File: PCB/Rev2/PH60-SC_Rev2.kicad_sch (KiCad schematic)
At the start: 44 parts, among them J1 USB_C_Receptacle_USB2.0_14P, J2 Conn_01x02_Pin, J3 Conn_01x02_Pin, U1 nRF52840, X1 32.768kHz, X2 Crystal_Generic

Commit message: Revert to production version and add back missing BOM
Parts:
- R1, R2: now in the parts list
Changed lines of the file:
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@@
 		(unit 1)
 		(exclude_from_sim no)
-		(in_bom no)
+		(in_bom yes)
 		(on_board yes)
 		(dnp no)
@@
 		(unit 1)
 		(exclude_from_sim no)
-		(in_bom no)
-		(on_board yes)
-		(dnp no)
+		(in_bom yes)
+		(on_board yes)
+		(dnp no)

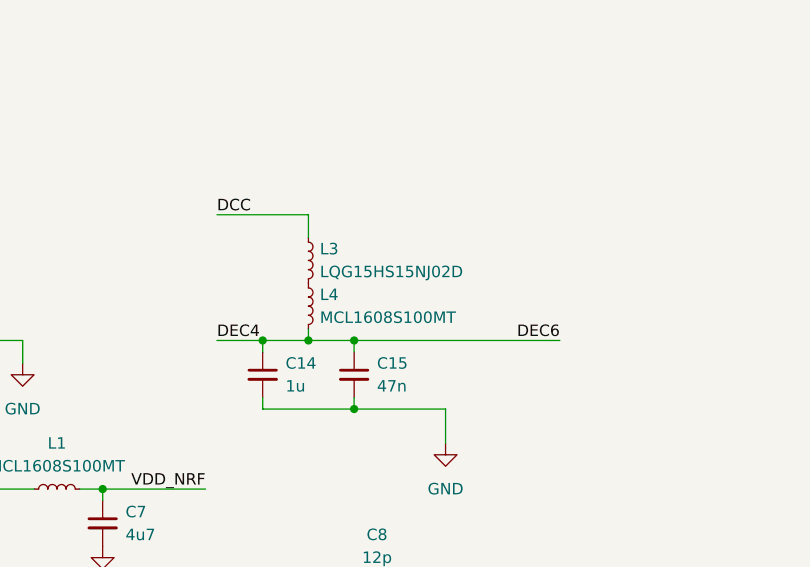
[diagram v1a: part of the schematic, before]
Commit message: Fix inductor order
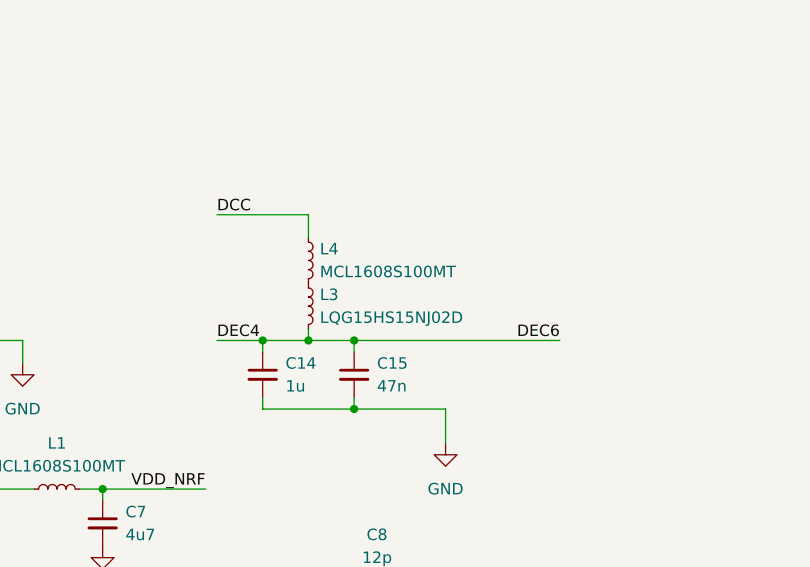
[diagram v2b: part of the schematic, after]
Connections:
- net DCC: now also L4.1; no longer L3.1
- net DEC4: now also L3.2; no longer L4.2
- new net: L3.1, L4.2
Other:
- moved on the sheet: L3, L4
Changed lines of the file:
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@@
 	(symbol
 		(lib_id "Device:L_Small")
-		(at 270.51 44.45 0)
+		(at 270.51 49.53 0)
 		(unit 1)
 		(exclude_from_sim no)
@@
 		(fields_autoplaced yes)
 		(property "Reference" "L3"
-			(at 271.78 43.1799 0)
+			(at 271.78 48.2599 0)
 			(effects
 				(font
@@
 		)
 		(property "Value" "LQG15HS15NJ02D"
-			(at 271.78 45.7199 0)
+			(at 271.78 50.7999 0)
 			(effects
 				(font
@@
 		)
 		(property "Footprint" "Inductor_SMD:L_0402_1005Metric"
-			(at 270.51 44.45 0)
+			(at 270.51 49.53 0)
 			(effects
 				(font
@@
 		)
 		(property "Datasheet" "~"
-			(at 270.51 44.45 0)
+			(at 270.51 49.53 0)
 			(effects
 				(font
@@
 		)
 		(property "Description" "Inductor, small symbol"
-			(at 270.51 44.45 0)
+			(at 270.51 49.53 0)
 			(effects
 				(font
@@
 		)
 		(instances
-			(project "PH64lite"
+			(project "PH60-SC_Rev2"
 				(path "/dca0f898-8fdb-4522-a51d-f4f4238906e7"
 					(reference "L3")
@@
 	(symbol
 		(lib_id "Device:L_Small")
-		(at 270.51 49.53 0)
+		(at 270.51 44.45 0)
 		(unit 1)
 		(exclude_from_sim no)
@@
 		(fields_autoplaced yes)
 		(property "Reference" "L4"
-			(at 271.78 48.2599 0)
+			(at 271.78 43.1799 0)
 			(effects
 				(font
@@
 		)
 		(property "Value" "MCL1608S100MT"
-			(at 271.78 50.7999 0)
+			(at 271.78 45.7199 0)
 			(effects
 				(font
@@
 		)
 		(property "Footprint" "Inductor_SMD:L_0603_1608Metric"
-			(at 270.51 49.53 0)
+			(at 270.51 44.45 0)
 			(effects
 				(font
@@
 		)
 		(property "Datasheet" "~"
-			(at 270.51 49.53 0)
+			(at 270.51 44.45 0)
 			(effects
 				(font
@@
 		)
 		(property "Description" "Inductor, small symbol"
-			(at 270.51 49.53 0)
+			(at 270.51 44.45 0)
 			(effects
 				(font
@@
 		)
 		(instances
-			(project "PH64lite"
+			(project "PH60-SC_Rev2"
 				(path "/dca0f898-8fdb-4522-a51d-f4f4238906e7"
 					(reference "L4")
